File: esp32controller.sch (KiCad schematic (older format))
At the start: 116 parts, among them J1 Conn_02x03_Odd_Even, J10 USB_B_Micro, J11 Conn_01x04_Female, J12 Conn_01x06_Female, J14 Conn_01x04, J15 Conn_01x06, J16 Conn_01x04, J17 Conn_01x04, J18 Conn_01x03, J19 Conn_01x03, J2 Conn_01x04, J20 Conn_01x03, J21 Conn_02x09_Odd_Even, J22 Conn_02x09_Odd_Even, J23 Conn_01x03, J24 Conn_01x03, J25 Conn_01x03, J26 Conn_02x09_Odd_Even, J3 Conn_02x03_Odd_Even, J4 Conn_01x04, J5 Conn_02x03_Odd_Even, J6 Conn_01x04, J7 Micro_SD_Card_Det, J8 Conn_02x03_Odd_Even, J9 Conn_01x04, Q1 Q_NPN_BEC, Q2 Q_NPN_BEC, Q3 Q_NMOS_GDS, Q4 Q_NMOS_GDS, Q5 Q_NMOS_GDS, U1 ESP32-WROOM, U2 CH340C, U3 ADS1015, U4 SX1509, U5 TPS560430, U6 TLV1117-33

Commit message: revision 2 with i2s schematic
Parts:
- removed C14, C15: 100nF, Capacitors_SMD:C_0603, symbol Device:C
- removed C16: 100n, Capacitors_SMD:C_0603, symbol Device:C
- removed C17: NC, Capacitors_SMD:C_0603, symbol Device:C
- removed J10: USB_B_Micro, ESP32Controller:473460001, symbol Connector:USB_B_Micro
- removed J16: Conn_01x04, Socket_Strips:Socket_Strip_Straight_2x02_Pitch2.54mm, symbol Connector_Generic:Conn_01x04
- removed J21, J22, J26: Conn_02x09_Odd_Even, Socket_Strips:Socket_Strip_Straight_2x09_Pitch2.54mm, symbol Connector_Generic:Conn_02x09_Odd_Even
- removed J23, J24, J25: Conn_01x03, Socket_Strips:Socket_Strip_Straight_1x03_Pitch2.54mm, symbol Connector_Generic:Conn_01x03
- removed R18: 10k, Resistors_SMD:R_0603, symbol Device:R
- removed R23, R24, R25, R26, R27, R28, R29, R30, R31, R32, R33, R34, R35: 0, Resistors_SMD:R_0603, symbol Device:R
- removed U3: ADS1015, Housings_SSOP:TSSOP-10_3x3mm_Pitch0.5mm, symbol ESP32Controller:ADS1015
- removed U4: SX1509, Housings_DFN_QFN:QFN-28-1EP_4x4mm_Pitch0.4mm, symbol ESP32Controller:SX1509
- added A?: Pololu_Breakout_A4988, Module:Pololu_Breakout-16_15.2x20.3mm, symbol esp32controller-rescue:Pololu_Breakout_A4988-Driver_Motor
- added C?: 10uF, Capacitors_SMD:C_0805, symbol Device:C
- added C? (x5): 0.1uF, symbol Device:C
- added C?: 100uF, Capacitors_SMD:CP_Elec_6.3x7.7, symbol esp32controller-rescue:CP-Device
- added C? (x2): NC, Capacitors_SMD:C_0603, symbol Device:C
- added J?: USB_B, symbol Connector:USB_B
- added J?: Conn_01x04, ESP32Controller:Socket_Strip_Straight_1x04_Pitch2.54mm_dual, symbol esp32controller-rescue:Conn_01x04-Connector_Generic
- added J?: Conn_02x03_Odd_Even, Socket_Strips:Socket_Strip_Straight_2x03_Pitch2.54mm, symbol esp32controller-rescue:Conn_02x03_Odd_Even-Connector_Generic
- added J?: Conn_01x06, Socket_Strips:Socket_Strip_Straight_1x06_Pitch2.54mm, symbol Connector_Generic:Conn_01x06
- added R?: 4.7k, Resistors_SMD:R_0603, symbol Device:R
- added R?: 100k, Resistors_SMD:R_0603, symbol esp32controller-rescue:R-Device
- added R? (x2): 0, symbol Device:R
- added R? (x2): 10k, Resistors_SMD:R_0603, symbol Device:R
- added U? (x4): 74HC595, symbol 74xx:74HC595
- J17: symbol Connector_Generic:Conn_01x04 -> Connector_Generic:Conn_01x06
- MK1, MK2, MK3, MK4: symbol Mechanical:Mounting_Hole -> esp32controller-rescue:Mounting_Hole-Mechanical
- U1: symbol ESP32-footprints-Shem-Lib:ESP32-WROOM -> esp32controller-rescue:ESP32-WROOM-ESP32-footprints-Shem-Lib
- U2: symbol ch34x:CH340G -> esp32controller-rescue:CH340G-ch34x
- U5: symbol ESP32Controller:TPS560430 -> esp32controller-rescue:TPS560430-ESP32Controller
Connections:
- net labels added: BCLK, HSPI_MISO, HSPI_MOSI, HSPI_SCK, HSPI_SS, Q0, Q1, Q10, Q11, Q12, Q13, Q14, Q15, Q16, Q17, Q18, Q19, Q2, Q20, Q21, Q22, Q23, Q24, Q25, Q26, Q27, Q28, Q29, Q3, Q30, Q31, Q4, Q5, Q6, Q7, Q8, Q9, SDI, SDO, SHIFT_VCC, THERM2, WCLK
- net labels removed: AIN0, AIN1, AIN2, AIN3, CLK, CMD, E0_DIR, E0_STEP, NINT, SD0, SD1, SD2, SD3, SEN, XIO0, XIO1, XIO10, XIO11, XIO12, XIO13, XIO14, XIO15, XIO2, XIO3, XIO4, XIO5, XIO6, XIO7, XIO8, XIO9, XOSCIO, X_DIR, X_MAX, X_STEP, Y_DIR, Y_MAX, Y_STEP, Z_DIR, Z_MAX, Z_STEP
- wire segments 361 -> 309
- no-connect marks 13 -> 18
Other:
- note added: "E1 STEPPER DRIVER"
- note added: "External debouncing circuit for the endstops\n(GPIO35 also doesn't contain an input pullup)"
- note added: "HSPI"
- note added: "Power this at 5V for the increased speed?"
- note added: "TODO lower these resistors"
- note added: "VSPI"
- note removed: "ADC"
- note removed: "GPIO Expander"
- note removed: "SPI"
- note removed: "Select if thermistor output goes\nto ESP32 or ADS1015"
- note removed: "i2c addresses\n00 0x3e\n01 0x3f\n10 0x70\n11 0x71"
- note removed: "i2c addresses\nGND 0x48\nVDD 0x49\nSDA 0x4A\nSCL 0x4B"
- note removed: "need external pullups for 34 and 35\nthese pins can only be inputs \nand don't have pull-up/down resistors"
- moved on the sheet: C1, C18, C3, R19

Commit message: improve schematic, fix footprints
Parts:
- removed J14: Conn_01x04, Socket_Strips:Socket_Strip_Straight_1x04_Pitch2.54mm, symbol Connector_Generic:Conn_01x04
- removed J15, J?: Conn_01x06, Socket_Strips:Socket_Strip_Straight_1x06_Pitch2.54mm, symbol Connector_Generic:Conn_01x06
- removed R? (x2): 0, symbol Device:R
- added C8: 100nF, Capacitor_SMD:C_0603_1608Metric, symbol Device:C
- added J6: Conn_02x16_Odd_Even, Connector_PinHeader_2.54mm:PinHeader_2x16_P2.54mm_Vertical, symbol Connector_Generic:Conn_02x16_Odd_Even
- added J8: Conn_01x32, Connector_PinHeader_2.54mm:PinHeader_2x16_P2.54mm_Vertical, symbol Connector_Generic:Conn_01x32
- added R28, R29, R30, R31: 10k, Resistor_SMD:R_0603_1608Metric, symbol esp32controller-rescue:R-Device
- added SW1: SW_Push, Button_Switch_SMD:SW_Push_1P1T_NO_6x6mm_H9.5mm, symbol Switch:SW_Push
- C1: renamed from C8; value 100n -> 100nF; footprint Capacitors_SMD:C_0603 -> Capacitor_SMD:C_0603_1608Metric
- C10, C11: renamed from C?; footprint Capacitors_SMD:C_0603 -> Capacitor_SMD:C_0603_1608Metric
- C12, C13, C14, C15, C20: renamed from C?; value 0.1uF -> 100nF; footprint (none) -> Capacitor_SMD:C_0603_1608Metric
- C16: renamed from C10; footprint Capacitors_SMD:CP_Elec_6.3x7.7 -> Capacitor_SMD:CP_Elec_6.3x7.7
- C17: renamed from C22; value 0.1uF -> 100nF; footprint Capacitors_SMD:C_0603 -> Capacitor_SMD:C_0603_1608Metric
- C18: renamed from C19; footprint Capacitors_SMD:C_0805 -> Capacitor_SMD:C_0805_2012Metric
- C19: renamed from C23; footprint Capacitors_SMD:C_0805 -> Capacitor_SMD:C_0805_2012Metric
- C2: renamed from C11; footprint Capacitors_SMD:C_0805 -> Capacitor_SMD:C_0805_2012Metric
- C21: renamed from C20; footprint Capacitors_SMD:C_0805 -> Capacitor_SMD:C_0805_2012Metric
- C22: renamed from C21; value 100uF -> 10uF; footprint Capacitors_SMD:C_0805 -> Capacitor_SMD:C_0805_2012Metric
- C23: renamed from C2; footprint Capacitors_SMD:CP_Elec_6.3x7.7 -> Capacitor_SMD:CP_Elec_6.3x7.7
- C24: renamed from C4; footprint Capacitors_SMD:CP_Elec_6.3x7.7 -> Capacitor_SMD:CP_Elec_6.3x7.7
- C25: renamed from C5; footprint Capacitors_SMD:CP_Elec_6.3x7.7 -> Capacitor_SMD:CP_Elec_6.3x7.7
- C26: renamed from C6; footprint Capacitors_SMD:CP_Elec_6.3x7.7 -> Capacitor_SMD:CP_Elec_6.3x7.7
- C27: renamed from C?; footprint Capacitors_SMD:CP_Elec_6.3x7.7 -> Capacitor_SMD:CP_Elec_6.3x7.7
- C3: renamed from C12; footprint Capacitors_SMD:C_0805 -> Capacitor_SMD:C_0805_2012Metric
- C4: renamed from C?; footprint Capacitors_SMD:C_0805 -> Capacitor_SMD:C_0805_2012Metric
- C5: renamed from C1; value 100uF -> 10uF; footprint Capacitors_SMD:C_0805 -> Capacitor_SMD:C_0805_2012Metric
- C6: renamed from C3; footprint Capacitors_SMD:C_0603 -> Capacitor_SMD:C_0603_1608Metric
- C7: renamed from C9; value 1nF -> 100nF; footprint Capacitors_SMD:C_0603 -> Capacitor_SMD:C_0603_1608Metric
- C9: renamed from C18; footprint Capacitors_SMD:C_0603 -> Capacitor_SMD:C_0603_1608Metric
- D1, D2: footprint Diodes_SMD:D_0603 -> Diode_SMD:D_0603_1608Metric
- D3: renamed from D4; footprint Diodes_SMD:D_0805 -> LED_SMD:LED_0805_2012Metric
- D4: renamed from D5; footprint Diodes_SMD:D_0805 -> LED_SMD:LED_0805_2012Metric
- D5: renamed from D6; footprint Diodes_SMD:D_0805 -> LED_SMD:LED_0805_2012Metric
- F1, F2: footprint ESP32Controller:FUSE -> ESP32Controller:Fuse_0679H
- J1: renamed from J17; value Conn_01x04 -> Conn_01x06; footprint Socket_Strips:Socket_Strip_Straight_2x02_Pitch2.54mm -> Connector_PinHeader_2.54mm:PinHeader_2x03_P2.54mm_Vertical
- J16: renamed from J1; footprint Socket_Strips:Socket_Strip_Straight_2x03_Pitch2.54mm -> Connector_PinHeader_2.54mm:PinHeader_2x03_P2.54mm_Vertical
- J17: renamed from J3; footprint Socket_Strips:Socket_Strip_Straight_2x03_Pitch2.54mm -> Connector_PinHeader_2.54mm:PinHeader_2x03_P2.54mm_Vertical
- J18: renamed from J5; footprint Socket_Strips:Socket_Strip_Straight_2x03_Pitch2.54mm -> Connector_PinHeader_2.54mm:PinHeader_2x03_P2.54mm_Vertical
- J19: renamed from J8; footprint Socket_Strips:Socket_Strip_Straight_2x03_Pitch2.54mm -> Connector_PinHeader_2.54mm:PinHeader_2x03_P2.54mm_Vertical
- J2: renamed from J?; footprint (none) -> Connector_USB:USB_B_OST_USB-B1HSxx_Horizontal
- J20: renamed from J?; footprint Socket_Strips:Socket_Strip_Straight_2x03_Pitch2.54mm -> Connector_PinHeader_2.54mm:PinHeader_2x03_P2.54mm_Vertical
- J3: renamed from J18; footprint Socket_Strips:Socket_Strip_Straight_1x03_Pitch2.54mm -> Connector_PinHeader_2.54mm:PinHeader_1x03_P2.54mm_Vertical
- J4: renamed from J19; footprint Socket_Strips:Socket_Strip_Straight_1x03_Pitch2.54mm -> Connector_PinHeader_2.54mm:PinHeader_1x03_P2.54mm_Vertical
- J5: renamed from J20; footprint Socket_Strips:Socket_Strip_Straight_1x03_Pitch2.54mm -> Connector_PinHeader_2.54mm:PinHeader_1x03_P2.54mm_Vertical
- J9: renamed from J7; symbol Connector:Micro_SD_Card_Det -> esp32controller-rescue:Micro_SD_Card_Det-Connector
- JP1: footprint Socket_Strips:Socket_Strip_Straight_1x03_Pitch2.54mm -> Connector_PinHeader_2.54mm:PinHeader_1x03_P2.54mm_Vertical
- MK1, MK2, MK3, MK4: footprint Mounting_Holes:MountingHole_3.2mm_M3 -> MountingHole:MountingHole_3.2mm_M3
- Q1, Q2: footprint TO_SOT_Packages_SMD:SOT-23 -> Package_TO_SOT_SMD:SOT-23
- Q3, Q4, Q5: footprint TO_SOT_Packages_SMD:TO-252-2 -> Package_TO_SOT_SMD:TO-252-2
- R1: renamed from R17; footprint Resistors_SMD:R_0603 -> Resistor_SMD:R_0603_1608Metric
- R10: renamed from R15; footprint Resistors_SMD:R_0603 -> Resistor_SMD:R_0603_1608Metric
- R11: renamed from R19; footprint Resistors_SMD:R_0603 -> Resistor_SMD:R_0603_1608Metric
- R12, R13, R3, R36: renamed from R?; footprint Resistors_SMD:R_0603 -> Resistor_SMD:R_0603_1608Metric
- R14: renamed from R21; footprint Resistors_SMD:R_0603 -> Resistor_SMD:R_0603_1608Metric
- R15: renamed from R22; footprint Resistors_SMD:R_0603 -> Resistor_SMD:R_0603_1608Metric
- R16: renamed from R38; value 1.5k -> 2.4k; footprint Resistors_SMD:R_1206 -> Resistor_SMD:R_1206_3216Metric
- R17: renamed from R39; value 1.5k -> 2.4k; footprint Resistors_SMD:R_1206 -> Resistor_SMD:R_1206_3216Metric
- R18: renamed from R9; footprint Resistors_SMD:R_0603 -> Resistor_SMD:R_0603_1608Metric
- R19: renamed from R10; footprint Resistors_SMD:R_0603 -> Resistor_SMD:R_0603_1608Metric
- R2: renamed from R20; footprint Resistors_SMD:R_0603 -> Resistor_SMD:R_0603_1608Metric
- R20: renamed from R11; footprint Resistors_SMD:R_0603 -> Resistor_SMD:R_0603_1608Metric
- R21: renamed from R12; footprint Resistors_SMD:R_0603 -> Resistor_SMD:R_0603_1608Metric
- R22: renamed from R36; footprint Resistors_SMD:R_0603 -> Resistor_SMD:R_0603_1608Metric
- R23: renamed from R13; footprint Resistors_SMD:R_0603 -> Resistor_SMD:R_0603_1608Metric
- R24: renamed from R37; footprint Resistors_SMD:R_0603 -> Resistor_SMD:R_0603_1608Metric
- R25: renamed from R14; footprint Resistors_SMD:R_0603 -> Resistor_SMD:R_0603_1608Metric
- R26: renamed from R40; footprint Resistors_SMD:R_0603 -> Resistor_SMD:R_0603_1608Metric
- R27: renamed from R1; footprint Resistors_SMD:R_0603 -> Resistor_SMD:R_0603_1608Metric
- R32: renamed from R2; footprint Resistors_SMD:R_0603 -> Resistor_SMD:R_0603_1608Metric
- R33: renamed from R4; footprint Resistors_SMD:R_0603 -> Resistor_SMD:R_0603_1608Metric
- R34: renamed from R6; footprint Resistors_SMD:R_0603 -> Resistor_SMD:R_0603_1608Metric
- R35: renamed from R8; footprint Resistors_SMD:R_0603 -> Resistor_SMD:R_0603_1608Metric
- R4: renamed from R7; value 12k -> 10k; footprint Resistors_SMD:R_0603 -> Resistor_SMD:R_0603_1608Metric
- R5: renamed from R16; footprint Resistors_SMD:R_0603 -> Resistor_SMD:R_0603_1608Metric
- R6: renamed from R3; footprint Resistors_SMD:R_0603 -> Resistor_SMD:R_0603_1608Metric
- R7: renamed from R41; footprint Resistors_SMD:R_0603 -> Resistor_SMD:R_0603_1608Metric
- R8: renamed from R5; footprint Resistors_SMD:R_0603 -> Resistor_SMD:R_0603_1608Metric
- R9: renamed from R42; footprint Resistors_SMD:R_0603 -> Resistor_SMD:R_0603_1608Metric
- U1: renamed from U2; footprint Housings_SSOP:SOP-16_4.4x10.4mm_Pitch1.27mm -> Package_SO:SOP-16_4.4x10.4mm_P1.27mm
- U3, U4, U5, U6: renamed from U?; footprint (none) -> Package_SO:TSSOP-16_4.4x5mm_P0.65mm
- U7: renamed from U5; footprint TO_SOT_Packages_SMD:SOT-23-6 -> Package_TO_SOT_SMD:SOT-23-6
- U8: renamed from U6; footprint TO_SOT_Packages_SMD:SOT-223-3_TabPin2 -> Package_TO_SOT_SMD:SOT-223-3_TabPin2
- gave numbers to parts that had none: 2
- renumbered J12 to J10, J2 to J11, J4 to J12, J6 to J13, J9 to J14, J11 to J7, U1 to U2
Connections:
- net labels removed: SHIFT_VCC
- wire segments 309 -> 355
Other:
- note added: "I2C SHIFT REGISTERS"
- note added: "Switch buttons"
- note removed: "HSPI"
- note removed: "Power this at 5V for the increased speed?"
- note removed: "TODO lower these resistors"
- note removed: "VSPI"
- moved on the sheet: C10, C11, C12, C13, C14, C15, C16, C7, C9, D3, D4, F1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

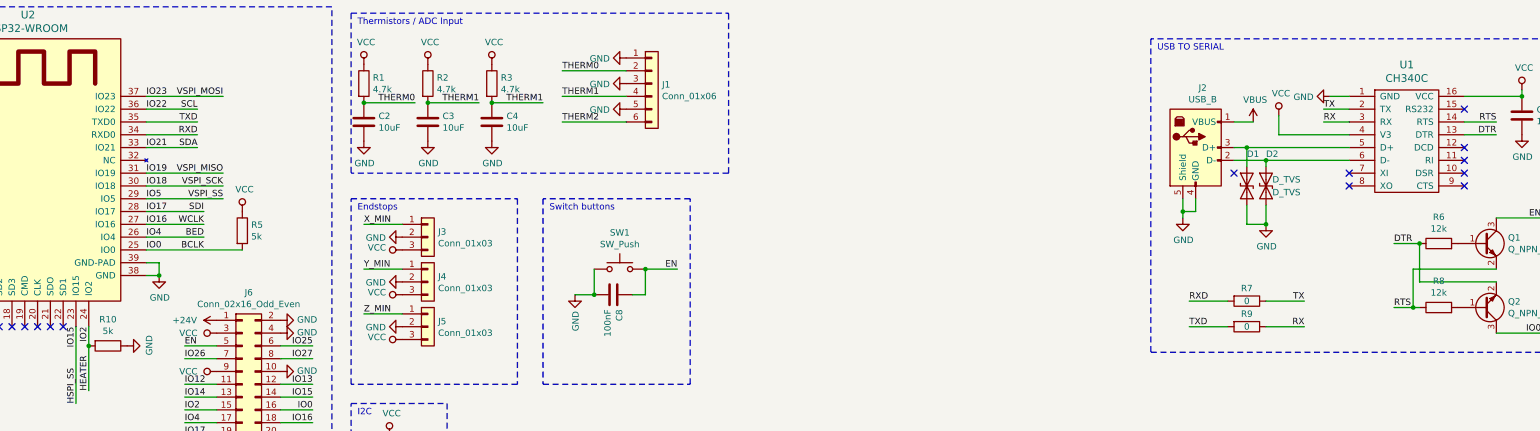
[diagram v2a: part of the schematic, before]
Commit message: tweaks
- use more consistent resitor values
- DNP R10, parallel with R21
- fix therm2 connection
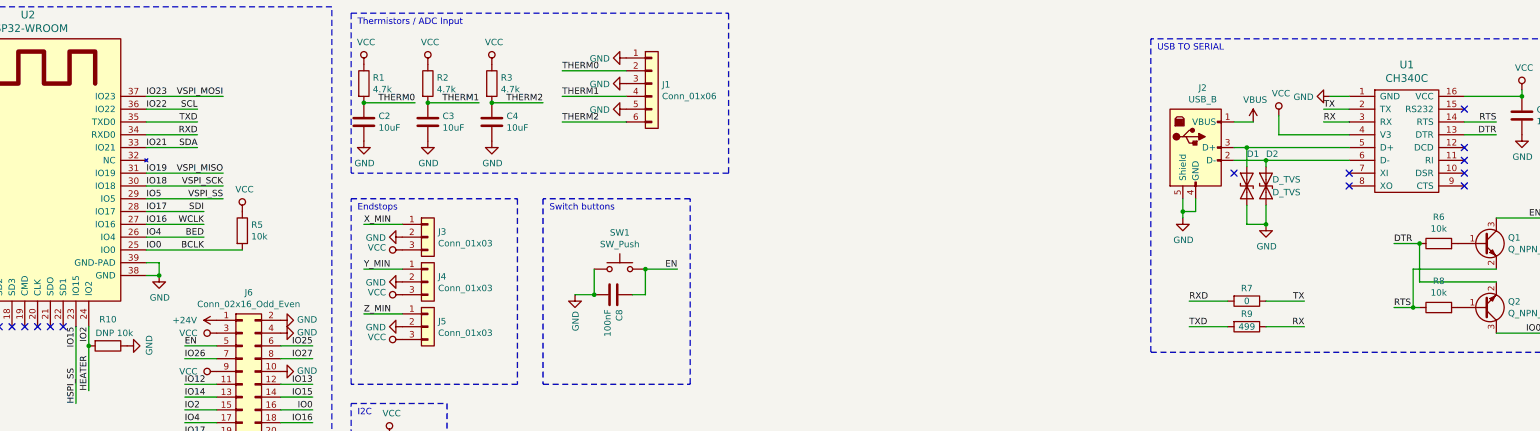
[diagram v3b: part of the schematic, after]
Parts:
- R10: value 5k -> DNP 10k
- R5: value 5k -> 10k
- R6, R8: value 12k -> 10k
- R9: value 0 -> 499
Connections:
- net IO34: now also C4.1, R3.2
- net SVN: no longer C4.1, R3.2
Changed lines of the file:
@@
 P 14600 2450
 F 0 "R6" V 14807 2450 50  0000 C CNN
-F 1 "12k" V 14716 2450 50  0000 C CNN
+F 1 "10k" V 14716 2450 50  0000 C CNN
 F 2 "Resistor_SMD:R_0603_1608Metric" V 14530 2450 50  0001 C CNN
 F 3 "~" H 14600 2450 50  0001 C CNN
@@
 P 14600 2950
 F 0 "R8" V 14807 2950 50  0000 C CNN
-F 1 "12k" V 14716 2950 50  0000 C CNN
+F 1 "10k" V 14716 2950 50  0000 C CNN
 F 2 "Resistor_SMD:R_0603_1608Metric" V 14530 2950 50  0001 C CNN
 F 3 "~" H 14600 2950 50  0001 C CNN
@@
 P 4200 3250
 F 0 "R10" V 3993 3250 50  0000 C CNN
-F 1 "5k" V 4084 3250 50  0000 C CNN
+F 1 "DNP 10k" V 4100 3300 50  0000 C CNN
 F 2 "Resistor_SMD:R_0603_1608Metric" V 4130 3250 50  0001 C CNN
 F 3 "~" H 4200 3250 50  0001 C CNN
@@
 P 5250 2350
 F 0 "R5" H 5320 2396 50  0000 L CNN
-F 1 "5k" H 5320 2305 50  0000 L CNN
+F 1 "10k" H 5320 2305 50  0000 L CNN
 F 2 "Resistor_SMD:R_0603_1608Metric" V 5180 2350 50  0001 C CNN
 F 3 "~" H 5250 2350 50  0001 C CNN
@@
 P 13100 3100
 F 0 "R9" V 13000 3100 50  0000 C CNN
-F 1 "0" V 13100 3100 50  0000 C CNN
+F 1 "499" V 13100 3100 50  0000 C CNN
 F 2 "Resistor_SMD:R_0603_1608Metric" V 13030 3100 50  0001 C CNN
 F 3 "~" H 13100 3100 50  0001 C CNN
@@
 $EndComp
 Text Label 7600 1350 2    50   ~ 0
-THERM1
+THERM2
 $Comp
 L Device:C C4

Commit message: added test points
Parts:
- added J21, J22, J23: Conn_01x01, Connector_PinHeader_2.54mm:PinHeader_1x01_P2.54mm_Vertical, symbol Connector_Generic:Conn_01x01
- added R37, R38, R39: 0, Resistor_SMD:R_0603_1608Metric, symbol Device:R
- added TP1, TP10, TP11, TP12, TP13, TP14, TP15, TP16, TP17, TP2, TP3, TP4, TP5, TP6, TP7, TP8, TP9: TestPoint, TestPoint:TestPoint_Plated_Hole_D2.0mm, symbol Connector:TestPoint
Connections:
- net +24V: now also TP14.1
- net +5V: now also TP15.1
- net BCLK: now also TP11.1, TP5.1
- net BED: now also R39.2; no longer R23.2, R25.2
- net DTR: now also TP2.1
- net EN: now also TP1.1
- net FAN: now also R37.2; no longer R18.2, R19.2
- net HEATER: now also R38.2; no longer R20.2, R21.2
- net IO16: now also TP12.1
- net IO17: now also TP7.1
- net RTS: now also TP4.1
- net RXD: now also TP3.1
- net SDO: now also TP13.1
- net TXD: now also TP6.1
- net VCC: now also TP17.1
- net at C21.1, JP1.2 (C), U8.3 (VI): now also TP16.1
- net at U3.9 (QH'), U4.14 (SER): now also TP8.1
- net at U4.9 (QH'), U5.14 (SER): now also TP9.1
- net at U5.9 (QH'), U6.14 (SER): now also TP10.1
- new net: J21.1 (Pin_1), R18.2, R19.2, R37.1
- new net: J22.1 (Pin_1), R20.2, R21.2, R38.1
- new net: J23.1 (Pin_1), R23.2, R25.2, R39.1
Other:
- moved on the sheet: Q1, Q2, Q3, Q4, Q5, R18, R19, R20, R21, R23, R25, R6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

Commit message: use loop footprint for testpoints
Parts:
- TP1, TP10, TP11, TP12, TP13, TP14, TP15, TP16, TP17, TP2, TP3, TP4, TP5, TP6, TP7, TP8, TP9: footprint TestPoint:TestPoint_Plated_Hole_D2.0mm -> TestPoint:TestPoint_Loop_D1.80mm_Drill1.0mm_Beaded
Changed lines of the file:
@@
 F 0 "TP14" H 1258 6572 50  0000 L CNN
 F 1 "TestPoint" H 1258 6527 50  0001 L CNN
-F 2 "TestPoint:TestPoint_Plated_Hole_D2.0mm" H 1400 6500 50  0001 C CNN
+F 2 "TestPoint:TestPoint_Loop_D1.80mm_Drill1.0mm_Beaded" H 1400 6500 50  0001 C CNN
 F 3 "~" H 1400 6500 50  0001 C CNN
 	1    1200 6500
@@
 F 0 "TP15" H 2908 6772 50  0000 L CNN
 F 1 "TestPoint" H 2908 6727 50  0001 L CNN
-F 2 "TestPoint:TestPoint_Plated_Hole_D2.0mm" H 3050 6700 50  0001 C CNN
+F 2 "TestPoint:TestPoint_Loop_D1.80mm_Drill1.0mm_Beaded" H 3050 6700 50  0001 C CNN
 F 3 "~" H 3050 6700 50  0001 C CNN
 	1    2850 6700
@@
 F 0 "TP16" H 1408 8122 50  0000 L CNN
 F 1 "TestPoint" H 1408 8077 50  0001 L CNN
-F 2 "TestPoint:TestPoint_Plated_Hole_D2.0mm" H 1550 8050 50  0001 C CNN
+F 2 "TestPoint:TestPoint_Loop_D1.80mm_Drill1.0mm_Beaded" H 1550 8050 50  0001 C CNN
 F 3 "~" H 1550 8050 50  0001 C CNN
 	1    1350 8050
@@
 F 0 "TP17" H 2358 8122 50  0000 L CNN
 F 1 "TestPoint" H 2358 8077 50  0001 L CNN
-F 2 "TestPoint:TestPoint_Plated_Hole_D2.0mm" H 2500 8050 50  0001 C CNN
+F 2 "TestPoint:TestPoint_Loop_D1.80mm_Drill1.0mm_Beaded" H 2500 8050 50  0001 C CNN
 F 3 "~" H 2500 8050 50  0001 C CNN
 	1    2300 8050
@@
 F 0 "TP2" H 14400 2550 50  0000 L CNN
 F 1 "TestPoint" H 14508 2377 50  0001 L CNN
-F 2 "TestPoint:TestPoint_Plated_Hole_D2.0mm" H 14650 2350 50  0001 C CNN
+F 2 "TestPoint:TestPoint_Loop_D1.80mm_Drill1.0mm_Beaded" H 14650 2350 50  0001 C CNN
 F 3 "~" H 14650 2350 50  0001 C CNN
 	1    14450 2350
@@
 F 0 "TP4" H 14350 3050 50  0000 L CNN
 F 1 "TestPoint" H 14458 2877 50  0001 L CNN
-F 2 "TestPoint:TestPoint_Plated_Hole_D2.0mm" H 14600 2850 50  0001 C CNN
+F 2 "TestPoint:TestPoint_Loop_D1.80mm_Drill1.0mm_Beaded" H 14600 2850 50  0001 C CNN
 F 3 "~" H 14600 2850 50  0001 C CNN
 	1    14400 2850
@@
 F 0 "TP3" H 12800 3000 50  0000 L CNN
 F 1 "TestPoint" H 12908 2827 50  0001 L CNN
-F 2 "TestPoint:TestPoint_Plated_Hole_D2.0mm" H 13050 2800 50  0001 C CNN
+F 2 "TestPoint:TestPoint_Loop_D1.80mm_Drill1.0mm_Beaded" H 13050 2800 50  0001 C CNN
 F 3 "~" H 13050 2800 50  0001 C CNN
 	1    12850 2800
@@
 F 0 "TP6" H 12800 3300 50  0000 L CNN
 F 1 "TestPoint" H 12908 3127 50  0001 L CNN
-F 2 "TestPoint:TestPoint_Plated_Hole_D2.0mm" H 13050 3100 50  0001 C CNN
+F 2 "TestPoint:TestPoint_Loop_D1.80mm_Drill1.0mm_Beaded" H 13050 3100 50  0001 C CNN
 F 3 "~" H 13050 3100 50  0001 C CNN
 	1    12850 3100
@@
 F 0 "TP1" H 15000 2350 50  0000 L CNN
 F 1 "TestPoint" H 15108 2177 50  0001 L CNN
-F 2 "TestPoint:TestPoint_Plated_Hole_D2.0mm" H 15250 2150 50  0001 C CNN
+F 2 "TestPoint:TestPoint_Loop_D1.80mm_Drill1.0mm_Beaded" H 15250 2150 50  0001 C CNN
 F 3 "~" H 15250 2150 50  0001 C CNN
 	1    15050 2150
@@
 F 0 "TP5" H 15000 3250 50  0000 L CNN
 F 1 "TestPoint" H 15108 3077 50  0001 L CNN
-F 2 "TestPoint:TestPoint_Plated_Hole_D2.0mm" H 15250 3050 50  0001 C CNN
+F 2 "TestPoint:TestPoint_Loop_D1.80mm_Drill1.0mm_Beaded" H 15250 3050 50  0001 C CNN
 F 3 "~" H 15250 3050 50  0001 C CNN
 	1    15050 3050
@@
 F 0 "TP7" H 10350 5500 50  0000 L CNN
 F 1 "TestPoint" H 10358 5427 50  0001 L CNN
-F 2 "TestPoint:TestPoint_Plated_Hole_D2.0mm" H 10500 5400 50  0001 C CNN
+F 2 "TestPoint:TestPoint_Loop_D1.80mm_Drill1.0mm_Beaded" H 10500 5400 50  0001 C CNN
 F 3 "~" H 10500 5400 50  0001 C CNN
 	1    10300 5400
@@
 F 0 "TP12" H 10350 6000 50  0000 L CNN
 F 1 "TestPoint" H 10358 5927 50  0001 L CNN
-F 2 "TestPoint:TestPoint_Plated_Hole_D2.0mm" H 10500 5900 50  0001 C CNN
+F 2 "TestPoint:TestPoint_Loop_D1.80mm_Drill1.0mm_Beaded" H 10500 5900 50  0001 C CNN
 F 3 "~" H 10500 5900 50  0001 C CNN
 	1    10300 5900
@@
 F 0 "TP11" H 10350 5700 50  0000 L CNN
 F 1 "TestPoint" H 10358 5627 50  0001 L CNN
-F 2 "TestPoint:TestPoint_Plated_Hole_D2.0mm" H 10500 5600 50  0001 C CNN
+F 2 "TestPoint:TestPoint_Loop_D1.80mm_Drill1.0mm_Beaded" H 10500 5600 50  0001 C CNN
 F 3 "~" H 10500 5600 50  0001 C CNN
 	1    10300 5600
@@
 F 0 "TP8" H 11650 5500 50  0000 L CNN
 F 1 "TestPoint" H 11658 5427 50  0001 L CNN
-F 2 "TestPoint:TestPoint_Plated_Hole_D2.0mm" H 11800 5400 50  0001 C CNN
+F 2 "TestPoint:TestPoint_Loop_D1.80mm_Drill1.0mm_Beaded" H 11800 5400 50  0001 C CNN
 F 3 "~" H 11800 5400 50  0001 C CNN
 	1    11600 5400
@@
 F 0 "TP9" H 13000 5500 50  0000 L CNN
 F 1 "TestPoint" H 13008 5427 50  0001 L CNN
-F 2 "TestPoint:TestPoint_Plated_Hole_D2.0mm" H 13150 5400 50  0001 C CNN
+F 2 "TestPoint:TestPoint_Loop_D1.80mm_Drill1.0mm_Beaded" H 13150 5400 50  0001 C CNN
 F 3 "~" H 13150 5400 50  0001 C CNN
 	1    12950 5400
@@
 F 0 "TP10" H 14350 5500 50  0000 L CNN
 F 1 "TestPoint" H 14358 5427 50  0001 L CNN
-F 2 "TestPoint:TestPoint_Plated_Hole_D2.0mm" H 14500 5400 50  0001 C CNN
+F 2 "TestPoint:TestPoint_Loop_D1.80mm_Drill1.0mm_Beaded" H 14500 5400 50  0001 C CNN
 F 3 "~" H 14500 5400 50  0001 C CNN
 	1    14300 5400
@@
 F 0 "TP13" H 15300 6400 50  0000 L CNN
 F 1 "TestPoint" H 15308 6327 50  0001 L CNN
-F 2 "TestPoint:TestPoint_Plated_Hole_D2.0mm" H 15450 6300 50  0001 C CNN
+F 2 "TestPoint:TestPoint_Loop_D1.80mm_Drill1.0mm_Beaded" H 15450 6300 50  0001 C CNN
 F 3 "~" H 15450 6300 50  0001 C CNN
 	1    15250 6300
